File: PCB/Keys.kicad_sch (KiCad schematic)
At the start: 0 parts

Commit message: switching to hall effect for now
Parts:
- added U? (x3): DRV5055A3xDBZxQ1, Package_TO_SOT_SMD:SOT-23, symbol Sensor_Magnetic:DRV5055A3xDBZxQ1
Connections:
- new net +3.3V: U?.1 (VCC), U?.1 (VCC), U?.1 (VCC)
- new net GND: U?.3 (GND), U?.3 (GND), U?.3 (GND)
- new net KEY1: U?.2 (OUT)
- new net KEY2: U?.2 (OUT)
- new net KEY3: U?.2 (OUT)

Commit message: cramming for portfolio
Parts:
- gave numbers to parts that had none: 3
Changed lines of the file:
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@@
 		(dnp no)
 		(fields_autoplaced yes)
-		(property "Reference" "U?"
+		(property "Reference" "U5"
 			(at 110.49 39.3699 0)
 			(effects
@@
 			(project "OTCboard"
 				(path "/f410b0a0-725c-464e-80be-c0074224226d/5b7118b6-76c9-4b8c-a9de-b6eee187afea"
-					(reference "U?")
+					(reference "U5")
 					(unit 1)
 				)
@@
 		(dnp no)
 		(fields_autoplaced yes)
-		(property "Reference" "#PWR012"
+		(property "Reference" "#PWR024"
 			(at 37.465 57.15 0)
 			(effects
@@
 			(project ""
 				(path "/f410b0a0-725c-464e-80be-c0074224226d/5b7118b6-76c9-4b8c-a9de-b6eee187afea"
-					(reference "#PWR012")
+					(reference "#PWR024")
 					(unit 1)
 				)
@@
 		(dnp no)
 		(fields_autoplaced yes)
-		(property "Reference" "#PWR015"
+		(property "Reference" "#PWR023"
 			(at 37.465 34.29 0)
 			(effects
@@
 			(project ""
 				(path "/f410b0a0-725c-464e-80be-c0074224226d/5b7118b6-76c9-4b8c-a9de-b6eee187afea"
-					(reference "#PWR015")
+					(reference "#PWR023")
 					(unit 1)
 				)
@@
 		(dnp no)
 		(fields_autoplaced yes)
-		(property "Reference" "U?"
+		(property "Reference" "U4"
 			(at 71.12 39.3699 0)
 			(effects
@@
 			(project "OTCboard"
 				(path "/f410b0a0-725c-464e-80be-c0074224226d/5b7118b6-76c9-4b8c-a9de-b6eee187afea"
-					(reference "U?")
+					(reference "U4")
 					(unit 1)
 				)
@@
 		(dnp no)
 		(fields_autoplaced yes)
-		(property "Reference" "#PWR013"
+		(property "Reference" "#PWR026"
 			(at 75.565 57.15 0)
 			(effects
@@
 			(project "OTCboard"
 				(path "/f410b0a0-725c-464e-80be-c0074224226d/5b7118b6-76c9-4b8c-a9de-b6eee187afea"
-					(reference "#PWR013")
+					(reference "#PWR026")
 					(unit 1)
 				)
@@
 		(dnp no)
 		(fields_autoplaced yes)
-		(property "Reference" "#PWR016"
+		(property "Reference" "#PWR025"
 			(at 75.565 34.29 0)
 			(effects
@@
 			(project "OTCboard"
 				(path "/f410b0a0-725c-464e-80be-c0074224226d/5b7118b6-76c9-4b8c-a9de-b6eee187afea"
-					(reference "#PWR016")
+					(reference "#PWR025")
 					(unit 1)
 				)
@@
 		(dnp no)
 		(fields_autoplaced yes)
-		(property "Reference" "#PWR014"
+		(property "Reference" "#PWR028"
 			(at 114.935 57.15 0)
 			(effects
@@
 			(project "OTCboard"
 				(path "/f410b0a0-725c-464e-80be-c0074224226d/5b7118b6-76c9-4b8c-a9de-b6eee187afea"
-					(reference "#PWR014")
+					(reference "#PWR028")
 					(unit 1)
 				)
@@
 		(dnp no)
 		(fields_autoplaced yes)
-		(property "Reference" "#PWR017"
+		(property "Reference" "#PWR027"
 			(at 114.935 34.29 0)
 			(effects
@@
 			(project "OTCboard"
 				(path "/f410b0a0-725c-464e-80be-c0074224226d/5b7118b6-76c9-4b8c-a9de-b6eee187afea"
-					(reference "#PWR017")
+					(reference "#PWR027")
 					(unit 1)
 				)
@@
 		(dnp no)
 		(fields_autoplaced yes)
-		(property "Reference" "U?"
+		(property "Reference" "U3"
 			(at 33.02 39.3699 0)
 			(effects
@@
 			(project ""
 				(path "/f410b0a0-725c-464e-80be-c0074224226d/5b7118b6-76c9-4b8c-a9de-b6eee187afea"
-					(reference "U?")
-					(unit 1)
-				)
+					(reference "U3")
+					(unit 1)
+				)

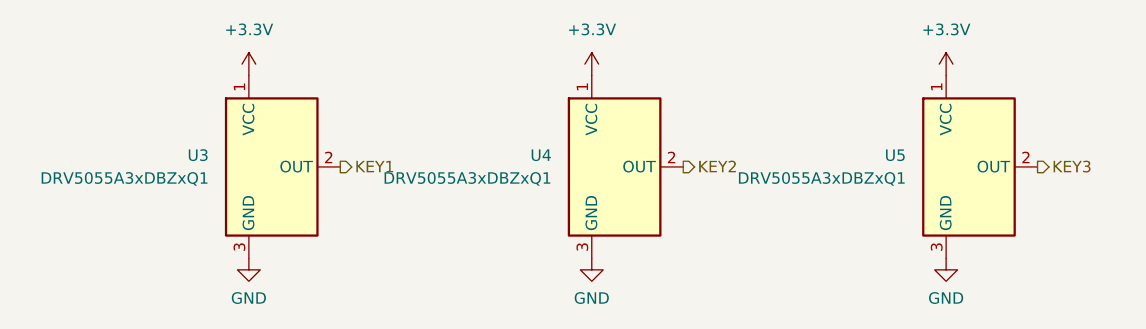
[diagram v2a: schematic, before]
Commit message: only need to find boot and reset footprints
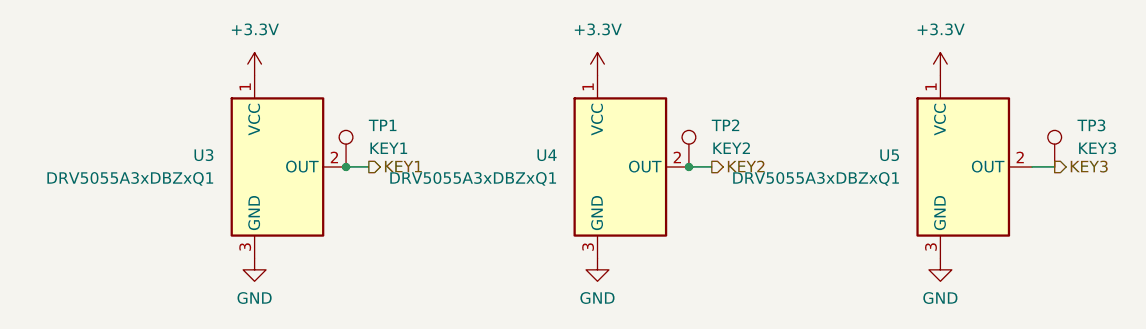
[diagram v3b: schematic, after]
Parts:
- added TP1: KEY1, TestPoint:TestPoint_Pad_2.0x2.0mm, symbol Connector:TestPoint
- added TP2: KEY2, TestPoint:TestPoint_Pad_2.0x2.0mm, symbol Connector:TestPoint
- added TP3: KEY3, TestPoint:TestPoint_Pad_2.0x2.0mm, symbol Connector:TestPoint
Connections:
- net KEY1: now also TP1.1
- net KEY2: now also TP2.1
- net KEY3: now also TP3.1
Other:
- moved on the sheet: U3, U4, U5

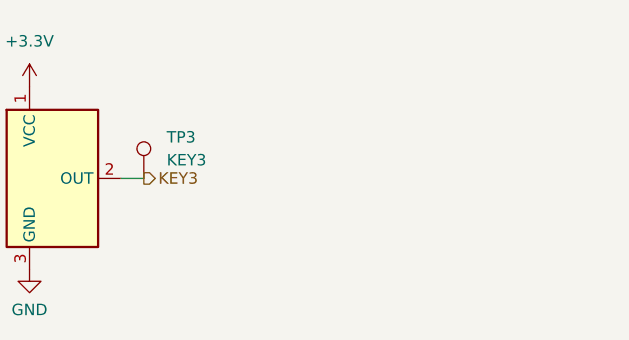
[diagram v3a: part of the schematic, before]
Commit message: changing to wasd
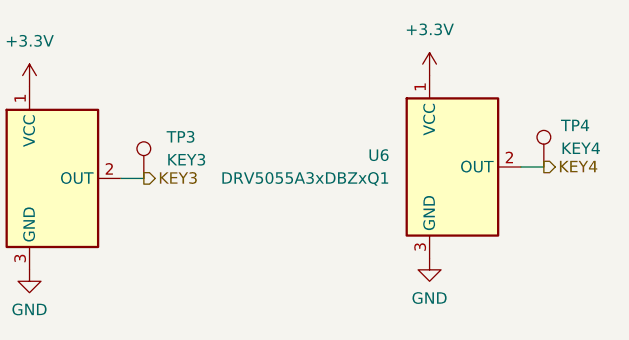
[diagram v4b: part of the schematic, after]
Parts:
- added TP4: KEY4, TestPoint:TestPoint_Pad_2.0x2.0mm, symbol Connector:TestPoint
- added U6: DRV5055A3xDBZxQ1, Package_TO_SOT_SMD:SOT-23, symbol Sensor_Magnetic:DRV5055A3xDBZxQ1
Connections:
- net +3.3V: now also U6.1 (VCC)
- net GND: now also U6.3 (GND)
- new net KEY4: TP4.1, U6.2 (OUT)

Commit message: new update
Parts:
- added C13, C14, C15, C16: 0.1u, Capacitor_SMD:C_0603_1608Metric_Pad1.08x0.95mm_HandSolder, symbol Device:C_Small
- TP3: renamed from TP1; footprint TestPoint:TestPoint_Pad_2.0x2.0mm -> TestPoint:TestPoint_Loop_D2.54mm_Drill1.5mm_Beaded
- TP4: renamed from TP2; footprint TestPoint:TestPoint_Pad_2.0x2.0mm -> TestPoint:TestPoint_Loop_D2.54mm_Drill1.5mm_Beaded
- TP5: renamed from TP3; footprint TestPoint:TestPoint_Pad_2.0x2.0mm -> TestPoint:TestPoint_Loop_D2.54mm_Drill1.5mm_Beaded
- TP6: renamed from TP4; footprint TestPoint:TestPoint_Pad_2.0x2.0mm -> TestPoint:TestPoint_Loop_D2.54mm_Drill1.5mm_Beaded
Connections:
- net +3.3V: now also C13.1, C14.1, C15.1, C16.1
- net GND: now also C13.2, C14.2, C15.2, C16.2
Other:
- note added: "Output Voltage Vout = Vq+B*(Sensitivity*(1+Stc*(Tambient-25C))) Vq=VCC/2=3.3/2=1.65 B=75Gs - 640 Gs = 7.5mT - 64mT Sensitivity = 15 mV/mT Stc = 0.0012 or 0.12% Tambient = 25C Vout = 1.765V - 2.639V"

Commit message: schematic done?
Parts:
- renumbered C13 to C14, C14 to C15, C15 to C16, C16 to C17
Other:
- moved on the sheet: C14, C15, C16

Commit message: analog signal design research
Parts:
- added C17, C18, C19, C21: 0.1u, Capacitor_SMD:C_0603_1608Metric_Pad1.08x0.95mm_HandSolder, symbol Device:C_Small
- added R10, R7, R8, R9: 1k, Resistor_SMD:R_0603_1608Metric_Pad0.98x0.95mm_HandSolder, symbol Device:R_US
- renumbered C17 to C20, U5 to U3, U3 to U4, U4 to U5
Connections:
- net GND: now also C17.2, C18.2, C19.2, C21.2; no longer U3.3 (GND), U4.3 (GND), U5.3 (GND), U6.3 (GND)
- net KEY1: now also C17.1, R7.2; no longer U4.2 (OUT)
- net KEY2: now also C18.1, R8.2; no longer U5.2 (OUT)
- net KEY3: now also C19.1, R9.2; no longer U3.2 (OUT)
- net KEY4: now also C21.1, R10.2; no longer U6.2 (OUT)
- net +3.3V renamed +3.3VA
- new net: R7.1, U4.2 (OUT)
- new net: R9.1, U3.2 (OUT)
- new net: R8.1, U5.2 (OUT)
- new net: R10.1, U6.2 (OUT)
- new net GNDA: U3.3 (GND), U4.3 (GND), U5.3 (GND), U6.3 (GND)
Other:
- note added: "Output Voltage Vout = Vq+B*(Sensitivity*(1+Stc*(Tambient-25C))) Vq=VCC/2=3.3/2=1.65 B=75Gs - 640 Gs = 7.5mT - 64mT Sensitivity = 15 mV/mT Stc = 0.0012 or 0.12% Tambient = 25C Vout = 1.765V - 2.639V Ripple = 3mVpp (datasheet) Filter: Fc=1/(2piRC) R=1000ohm, F=1Hz C=1/(2piRF)=0.1667uF just use C=0.luF -> F=1592Hz"
- note removed: "Output Voltage Vout = Vq+B*(Sensitivity*(1+Stc*(Tambient-25C))) Vq=VCC/2=3.3/2=1.65 B=75Gs - 640 Gs = 7.5mT - 64mT Sensitivity = 15 mV/mT Stc = 0.0012 or 0.12% Tambient = 25C Vout = 1.765V - 2.639V"
- moved on the sheet: C15, C16, TP3, TP4, TP5, TP6, U3, U5
